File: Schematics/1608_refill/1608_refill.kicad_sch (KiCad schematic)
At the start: 67 parts, among them J1 USB_B_Micro, J10 Switch 2, J11 Switch 3, J12 Switch 1, J13 SWD, J14 SWD, J15 Screen data, J16 Screen Backlight, J2 Pot 1, J3 Barrel_Jack_Switch, J4 USB_BOOT, J5 Load Cell Power, J6 Load Cell Data, J7 Inductor 1, J8 Inductor 2, J9 Pot 2, Q1 TIP120, Q2 TIP120, SW4 SW_SPDT, U1 RP2040, U2 NCP1117-3.3_SOT223, U3 Flash Memory, U5 AD622, Y1 Crystal

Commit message: gearing up for PCB 2
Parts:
- added R17, R18: 200, Resistor_SMD:R_0603_1608Metric_Pad0.98x0.95mm_HandSolder, symbol Device:R
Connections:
- net P1: now also R18.2; no longer J2.2 (Pin_2)
- net P2: now also R17.2; no longer J9.2 (Pin_2)
- new net: J9.2 (Pin_2), R17.1
- new net: J2.2 (Pin_2), R18.1
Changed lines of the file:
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@@
 (kicad_sch (version 20211123) (generator eeschema)
   (paper "A3")
+  (junction (at 69.215 218.44) (diameter 0) (color 0 0 0 0)
+  )
   (junction (at 194.31 157.48) (diameter 0) (color 0 0 0 0)
   )
-  (junction (at 69.85 214.63) (diameter 0) (color 0 0 0 0)
-  )
   (junction (at 251.46 63.5) (diameter 0) (color 0 0 0 0)
   )
@@
     (stroke (width 0) (type default) (color 0 0 0 0))
   )
+  (wire (pts (xy 58.42 209.55) (xy 69.215 209.55))
+    (stroke (width 0) (type default) (color 0 0 0 0))
+  )
   (wire (pts (xy 134.62 124.46) (xy 135.89 124.46))
     (stroke (width 0) (type default) (color 0 0 0 0))
@@
     (stroke (width 0) (type default) (color 0 0 0 0))
   )
+  (wire (pts (xy 69.215 209.55) (xy 69.215 218.44))
+    (stroke (width 0) (type default) (color 0 0 0 0))
+  )
   (wire (pts (xy 113.03 236.22) (xy 124.46 236.22))
     (stroke (width 0) (type default) (color 0 0 0 0))
@@
     (stroke (width 0) (type default) (color 0 0 0 0))
   )
+  (wire (pts (xy 91.44 207.01) (xy 95.25 207.01))
+    (stroke (width 0) (type default) (color 0 0 0 0))
+  )
   (wire (pts (xy 222.25 63.5) (xy 222.25 81.28))
     (stroke (width 0) (type default) (color 0 0 0 0))
@@
     (stroke (width 0) (type default) (color 0 0 0 0))
   )
-  (wire (pts (xy 58.42 209.55) (xy 58.42 214.63))
-    (stroke (width 0) (type default) (color 0 0 0 0))
-  )
   (wire (pts (xy 45.72 20.32) (xy 49.53 20.32))
     (stroke (width 0) (type default) (color 0 0 0 0))
@@
     (stroke (width 0) (type default) (color 0 0 0 0))
   )
-  (wire (pts (xy 58.42 214.63) (xy 69.85 214.63))
-    (stroke (width 0) (type default) (color 0 0 0 0))
-  )
-  (wire (pts (xy 69.85 214.63) (xy 81.28 214.63))
-    (stroke (width 0) (type default) (color 0 0 0 0))
-  )
   (wire (pts (xy 273.05 63.5) (xy 287.02 63.5))
     (stroke (width 0) (type default) (color 0 0 0 0))
@@
     (stroke (width 0) (type default) (color 0 0 0 0))
   )
+  (wire (pts (xy 81.28 209.55) (xy 81.28 218.44))
+    (stroke (width 0) (type default) (color 0 0 0 0))
+  )
   (wire (pts (xy 44.45 251.46) (xy 44.45 250.19))
     (stroke (width 0) (type default) (color 0 0 0 0))
@@
     (stroke (width 0) (type default) (color 0 0 0 0))
   )
-  (wire (pts (xy 58.42 207.01) (xy 62.23 207.01))
-    (stroke (width 0) (type default) (color 0 0 0 0))
-  )
   (wire (pts (xy 261.62 71.12) (xy 264.16 71.12))
     (stroke (width 0) (type default) (color 0 0 0 0))
@@
     (stroke (width 0) (type default) (color 0 0 0 0))
   )
+  (wire (pts (xy 81.28 207.01) (xy 83.82 207.01))
+    (stroke (width 0) (type default) (color 0 0 0 0))
+  )
   (wire (pts (xy 340.36 54.61) (xy 340.36 59.69))
     (stroke (width 0) (type default) (color 0 0 0 0))
@@
     (stroke (width 0) (type default) (color 0 0 0 0))
   )
+  (wire (pts (xy 81.28 218.44) (xy 69.215 218.44))
+    (stroke (width 0) (type default) (color 0 0 0 0))
+  )
   (wire (pts (xy 167.64 251.46) (xy 172.72 251.46))
     (stroke (width 0) (type default) (color 0 0 0 0))
@@
     (stroke (width 0) (type default) (color 0 0 0 0))
   )
-  (wire (pts (xy 81.28 209.55) (xy 81.28 214.63))
-    (stroke (width 0) (type default) (color 0 0 0 0))
-  )
   (wire (pts (xy 58.42 200.66) (xy 58.42 204.47))
     (stroke (width 0) (type default) (color 0 0 0 0))
@@
     (stroke (width 0) (type default) (color 0 0 0 0))
   )
+  (wire (pts (xy 67.945 207.01) (xy 69.85 207.01))
+    (stroke (width 0) (type default) (color 0 0 0 0))
+  )
   (wire (pts (xy 176.53 157.48) (xy 176.53 156.21))
     (stroke (width 0) (type default) (color 0 0 0 0))
@@
   )
   (wire (pts (xy 312.42 106.68) (xy 316.23 106.68))
+    (stroke (width 0) (type default) (color 0 0 0 0))
+  )
+  (wire (pts (xy 58.42 207.01) (xy 60.325 207.01))
     (stroke (width 0) (type default) (color 0 0 0 0))
   )
@@
     (effects (font (size 1.27 1.27)) (justify left bottom))
   )
-  (label "P2" (at 81.28 207.01 0)
+  (label "P2" (at 95.25 207.01 0)
     (effects (font (size 1.27 1.27)) (justify left bottom))
   )
@@
     (effects (font (size 1.27 1.27)) (justify left bottom))
   )
-  (label "P1" (at 62.23 207.01 0)
+  (label "P1" (at 69.85 207.01 0)
     (effects (font (size 1.27 1.27)) (justify left bottom))
   )
@@
     (pin "1")
   )
+  (symbol (lib_id "Device:R") (at 87.63 207.01 90) (unit 1)
+    (in_bom yes) (on_board yes) (fields_autoplaced)
+    (property "Reference" "R17" (id 0) (at 86.3599 205.105 0)
+      (effects (font (size 1.27 1.27)) (justify left))
+    )
+    (property "Value" "200" (id 1) (at 88.8999 205.105 0)
+      (effects (font (size 1.27 1.27)) (justify left))
+    )
+    (property "Footprint" "Resistor_SMD:R_0603_1608Metric_Pad0.98x0.95mm_HandSolder" (id 2) (at 87.63 208.788 90)
+      (effects (font (size 1.27 1.27)) hide)
+    )
+    (property "Datasheet" "~" (id 3) (at 87.63 207.01 0)
+      (effects (font (size 1.27 1.27)) hide)
+    )
+    (pin "1")
+    (pin "2")
+  )
   (symbol (lib_id "Connector:Screw_Terminal_01x02") (at 335.28 52.07 180) (unit 1)
     (in_bom yes) (on_board yes) (fields_autoplaced)
@@
     (pin "1")
   )
-  (symbol (lib_id "power:GND") (at 69.85 214.63 0) (unit 1)
-    (in_bom yes) (on_board yes) (fields_autoplaced)
-    (property "Reference" "#PWR0122" (id 0) (at 69.85 220.98 0)
-      (effects (font (size 1.27 1.27)) hide)
-    )
-    (property "Value" "GND" (id 1) (at 69.85 219.075 0))
-    (property "Footprint" "" (id 2) (at 69.85 214.63 0)
-      (effects (font (size 1.27 1.27)) hide)
-    )
-    (property "Datasheet" "" (id 3) (at 69.85 214.63 0)
+  (symbol (lib_id "power:GND") (at 69.215 218.44 0) (unit 1)
+    (in_bom yes) (on_board yes) (fields_autoplaced)
+    (property "Reference" "#PWR0122" (id 0) (at 69.215 224.79 0)
+      (effects (font (size 1.27 1.27)) hide)
+    )
+    (property "Value" "GND" (id 1) (at 69.215 222.885 0))
+    (property "Footprint" "" (id 2) (at 69.215 218.44 0)
+      (effects (font (size 1.27 1.27)) hide)
+    )
+    (property "Datasheet" "" (id 3) (at 69.215 218.44 0)
       (effects (font (size 1.27 1.27)) hide)
     )
@@
     )
     (pin "1")
+  )
+  (symbol (lib_id "Device:R") (at 64.135 207.01 90) (unit 1)
+    (in_bom yes) (on_board yes)
+    (property "Reference" "R18" (id 0) (at 64.135 203.2 90))
+    (property "Value" "200" (id 1) (at 64.135 205.105 90))
+    (property "Footprint" "Resistor_SMD:R_0603_1608Metric_Pad0.98x0.95mm_HandSolder" (id 2) (at 64.135 208.788 90)
+      (effects (font (size 1.27 1.27)) hide)
+    )
+    (property "Datasheet" "~" (id 3) (at 64.135 207.01 0)
+      (effects (font (size 1.27 1.27)) hide)
+    )
+    (pin "1")
+    (pin "2")
   )
   (symbol (lib_id "power:GND") (at 91.44 254 90) (unit 1)
@@
       (reference "R16") (unit 1) (value "10k") (footprint "Resistor_SMD:R_0603_1608Metric_Pad0.98x0.95mm_HandSolder")
     )
+    (path "/21a5ca2a-fedc-4335-aaa7-0ee9a570b8e4"
+      (reference "R17") (unit 1) (value "200") (footprint "Resistor_SMD:R_0603_1608Metric_Pad0.98x0.95mm_HandSolder")
+    )
+    (path "/7460e61c-19d0-4033-b09e-2889e4259a28"
+      (reference "R18") (unit 1) (value "200") (footprint "Resistor_SMD:R_0603_1608Metric_Pad0.98x0.95mm_HandSolder")
+    )
     (path "/97d684aa-94d0-49de-b3b8-cdc9d921bb6e"

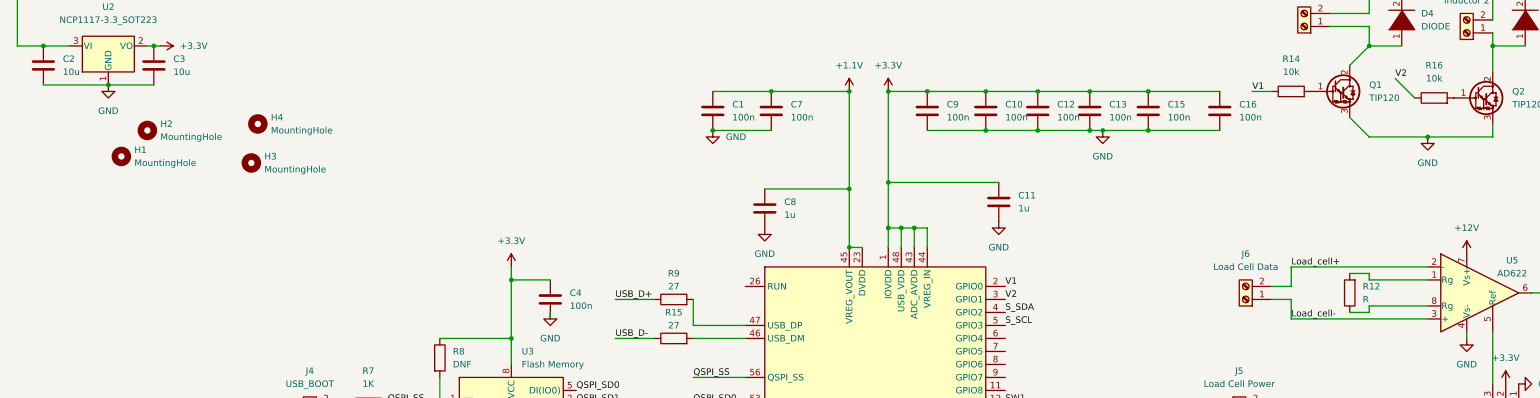
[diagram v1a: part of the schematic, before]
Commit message: 1608:all routes connected
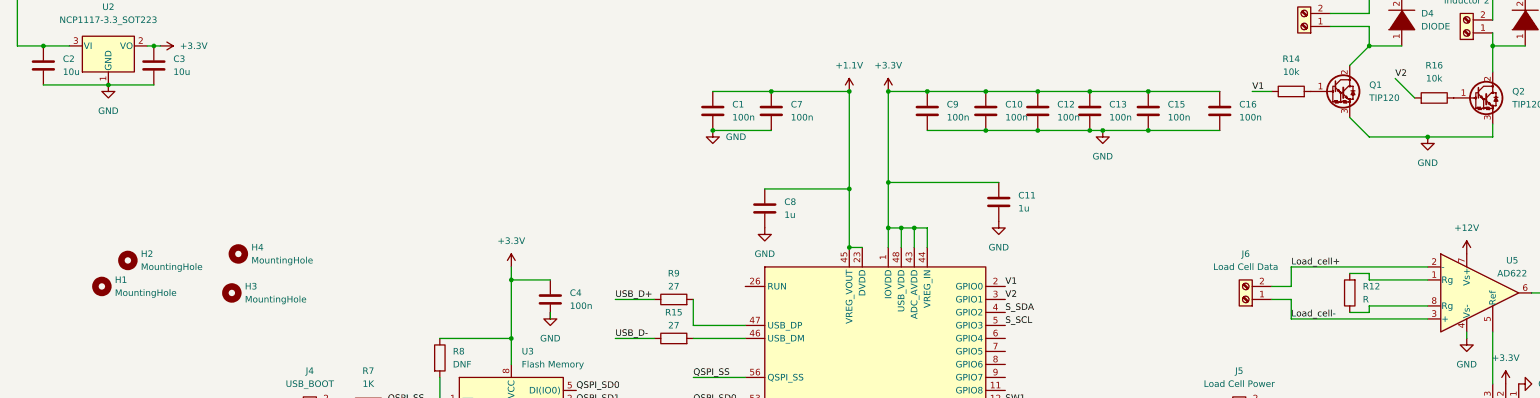
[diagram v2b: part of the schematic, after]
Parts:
- Y1: footprint Crystal:Crystal_SMD_SeikoEpson_MA505-2Pin_12.7x5.1mm_HandSoldering -> Library:ABLS12MHZ
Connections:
- net V2: now also R16.2; no longer R16.1
- net at Q2.1 (B): now also R16.1; no longer R16.2
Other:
- moved on the sheet: H1, H2, H3, H4, R16
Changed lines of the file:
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@@
     (pin "2")
   )
-  (symbol (lib_id "Mechanical:MountingHole") (at 77.47 71.12 0) (unit 1)
-    (in_bom yes) (on_board yes) (fields_autoplaced)
-    (property "Reference" "H2" (id 0) (at 80.01 69.8499 0)
-      (effects (font (size 1.27 1.27)) (justify left))
-    )
-    (property "Value" "MountingHole" (id 1) (at 80.01 72.3899 0)
-      (effects (font (size 1.27 1.27)) (justify left))
-    )
-    (property "Footprint" "MountingHole:MountingHole_2.1mm" (id 2) (at 77.47 71.12 0)
-      (effects (font (size 1.27 1.27)) hide)
-    )
-    (property "Datasheet" "~" (id 3) (at 77.47 71.12 0)
+  (symbol (lib_id "Mechanical:MountingHole") (at 73.66 96.52 0) (unit 1)
+    (in_bom yes) (on_board yes) (fields_autoplaced)
+    (property "Reference" "H2" (id 0) (at 76.2 95.2499 0)
+      (effects (font (size 1.27 1.27)) (justify left))
+    )
+    (property "Value" "MountingHole" (id 1) (at 76.2 97.7899 0)
+      (effects (font (size 1.27 1.27)) (justify left))
+    )
+    (property "Footprint" "MountingHole:MountingHole_2.1mm" (id 2) (at 73.66 96.52 0)
+      (effects (font (size 1.27 1.27)) hide)
+    )
+    (property "Datasheet" "~" (id 3) (at 73.66 96.52 0)
       (effects (font (size 1.27 1.27)) hide)
     )
@@
     (pin "1")
   )
-  (symbol (lib_id "Mechanical:MountingHole") (at 97.79 77.47 0) (unit 1)
-    (in_bom yes) (on_board yes) (fields_autoplaced)
-    (property "Reference" "H3" (id 0) (at 100.33 76.1999 0)
-      (effects (font (size 1.27 1.27)) (justify left))
-    )
-    (property "Value" "MountingHole" (id 1) (at 100.33 78.7399 0)
-      (effects (font (size 1.27 1.27)) (justify left))
-    )
-    (property "Footprint" "MountingHole:MountingHole_2.1mm" (id 2) (at 97.79 77.47 0)
-      (effects (font (size 1.27 1.27)) hide)
-    )
-    (property "Datasheet" "~" (id 3) (at 97.79 77.47 0)
+  (symbol (lib_id "Mechanical:MountingHole") (at 93.98 102.87 0) (unit 1)
+    (in_bom yes) (on_board yes) (fields_autoplaced)
+    (property "Reference" "H3" (id 0) (at 96.52 101.5999 0)
+      (effects (font (size 1.27 1.27)) (justify left))
+    )
+    (property "Value" "MountingHole" (id 1) (at 96.52 104.1399 0)
+      (effects (font (size 1.27 1.27)) (justify left))
+    )
+    (property "Footprint" "MountingHole:MountingHole_2.1mm" (id 2) (at 93.98 102.87 0)
+      (effects (font (size 1.27 1.27)) hide)
+    )
+    (property "Datasheet" "~" (id 3) (at 93.98 102.87 0)
       (effects (font (size 1.27 1.27)) hide)
     )
@@
     (pin "1")
   )
-  (symbol (lib_id "Mechanical:MountingHole") (at 99.06 69.85 0) (unit 1)
-    (in_bom yes) (on_board yes) (fields_autoplaced)
-    (property "Reference" "H4" (id 0) (at 101.6 68.5799 0)
-      (effects (font (size 1.27 1.27)) (justify left))
-    )
-    (property "Value" "MountingHole" (id 1) (at 101.6 71.1199 0)
-      (effects (font (size 1.27 1.27)) (justify left))
-    )
-    (property "Footprint" "MountingHole:MountingHole_2.1mm" (id 2) (at 99.06 69.85 0)
-      (effects (font (size 1.27 1.27)) hide)
-    )
-    (property "Datasheet" "~" (id 3) (at 99.06 69.85 0)
+  (symbol (lib_id "Mechanical:MountingHole") (at 95.25 95.25 0) (unit 1)
+    (in_bom yes) (on_board yes) (fields_autoplaced)
+    (property "Reference" "H4" (id 0) (at 97.79 93.9799 0)
+      (effects (font (size 1.27 1.27)) (justify left))
+    )
+    (property "Value" "MountingHole" (id 1) (at 97.79 96.5199 0)
+      (effects (font (size 1.27 1.27)) (justify left))
+    )
+    (property "Footprint" "MountingHole:MountingHole_2.1mm" (id 2) (at 95.25 95.25 0)
+      (effects (font (size 1.27 1.27)) hide)
+    )
+    (property "Datasheet" "~" (id 3) (at 95.25 95.25 0)
       (effects (font (size 1.27 1.27)) hide)
     )
@@
     (pin "1")
   )
-  (symbol (lib_id "Device:R") (at 328.93 64.77 90) (unit 1)
+  (symbol (lib_id "Device:R") (at 328.93 64.77 270) (mirror x) (unit 1)
     (in_bom yes) (on_board yes) (fields_autoplaced)
     (property "Reference" "R16" (id 0) (at 328.93 58.42 90))
@@
     (pin "2")
   )
-  (symbol (lib_id "Mechanical:MountingHole") (at 72.39 76.2 0) (unit 1)
-    (in_bom yes) (on_board yes) (fields_autoplaced)
-    (property "Reference" "H1" (id 0) (at 74.93 74.9299 0)
-      (effects (font (size 1.27 1.27)) (justify left))
-    )
-    (property "Value" "MountingHole" (id 1) (at 74.93 77.4699 0)
-      (effects (font (size 1.27 1.27)) (justify left))
-    )
-    (property "Footprint" "MountingHole:MountingHole_2.1mm" (id 2) (at 72.39 76.2 0)
-      (effects (font (size 1.27 1.27)) hide)
-    )
-    (property "Datasheet" "~" (id 3) (at 72.39 76.2 0)
+  (symbol (lib_id "Mechanical:MountingHole") (at 68.58 101.6 0) (unit 1)
+    (in_bom yes) (on_board yes) (fields_autoplaced)
+    (property "Reference" "H1" (id 0) (at 71.12 100.3299 0)
+      (effects (font (size 1.27 1.27)) (justify left))
+    )
+    (property "Value" "MountingHole" (id 1) (at 71.12 102.8699 0)
+      (effects (font (size 1.27 1.27)) (justify left))
+    )
+    (property "Footprint" "MountingHole:MountingHole_2.1mm" (id 2) (at 68.58 101.6 0)
+      (effects (font (size 1.27 1.27)) hide)
+    )
+    (property "Datasheet" "~" (id 3) (at 68.58 101.6 0)
       (effects (font (size 1.27 1.27)) hide)
     )
@@
       (effects (font (size 1.27 1.27)) (justify right))
     )
-    (property "Footprint" "Crystal:Crystal_SMD_SeikoEpson_MA505-2Pin_12.7x5.1mm_HandSoldering" (id 2) (at 176.53 152.4 0)
+    (property "Footprint" "Library:ABLS12MHZ" (id 2) (at 176.53 152.4 0)
       (effects (font (size 1.27 1.27)) hide)
     )
@@
     )
     (path "/c08205c4-4242-4490-8e8c-2116eeb68ea6"
-      (reference "Y1") (unit 1) (value "Crystal") (footprint "Crystal:Crystal_SMD_SeikoEpson_MA505-2Pin_12.7x5.1mm_HandSoldering")
-    )
-  )
+      (reference "Y1") (unit 1) (value "Crystal") (footprint "Library:ABLS12MHZ")
+    )
+  )

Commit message: 1608 mostly done
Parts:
- R12: footprint Resistor_THT:R_Axial_DIN0204_L3.6mm_D1.6mm_P2.54mm_Vertical -> Resistor_THT:R_Axial_DIN0204_L3.6mm_D1.6mm_P7.62mm_Horizontal
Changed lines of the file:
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@@
   (junction (at 261.62 71.12) (diameter 0) (color 0 0 0 0)
   )
-  (junction (at 20.32 242.57) (diameter 0) (color 0 0 0 0)
-  )
   (junction (at 187.96 71.12) (diameter 0) (color 0 0 0 0)
   )
@@
   )
   (wire (pts (xy 300.99 101.6) (xy 300.99 97.79))
-    (stroke (width 0) (type default) (color 0 0 0 0))
-  )
-  (wire (pts (xy 20.32 242.57) (xy 20.32 242.5959))
     (stroke (width 0) (type default) (color 0 0 0 0))
   )
@@
       (effects (font (size 1.27 1.27)) (justify right))
     )
-    (property "Footprint" "Resistor_THT:R_Axial_DIN0204_L3.6mm_D1.6mm_P2.54mm_Vertical" (id 2) (at 314.198 102.87 90)
+    (property "Footprint" "Resistor_THT:R_Axial_DIN0204_L3.6mm_D1.6mm_P7.62mm_Horizontal" (id 2) (at 314.198 102.87 90)
       (effects (font (size 1.27 1.27)) hide)
     )
@@
     )
     (path "/a8723716-a391-499a-8a65-65ccfccc4a94"
-      (reference "R12") (unit 1) (value "R") (footprint "Resistor_THT:R_Axial_DIN0204_L3.6mm_D1.6mm_P2.54mm_Vertical")
+      (reference "R12") (unit 1) (value "R") (footprint "Resistor_THT:R_Axial_DIN0204_L3.6mm_D1.6mm_P7.62mm_Horizontal")
     )
     (path "/f077b1ab-a878-4e03-8124-99be44917f25"
